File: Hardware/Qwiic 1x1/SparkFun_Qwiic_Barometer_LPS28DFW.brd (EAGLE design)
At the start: 25.4 x 25.4 mm, 48 parts, among them J1 QWIIC_RIGHT_ANGLE, J2 QWIIC_RIGHT_ANGLE, U1 LPS28DFW

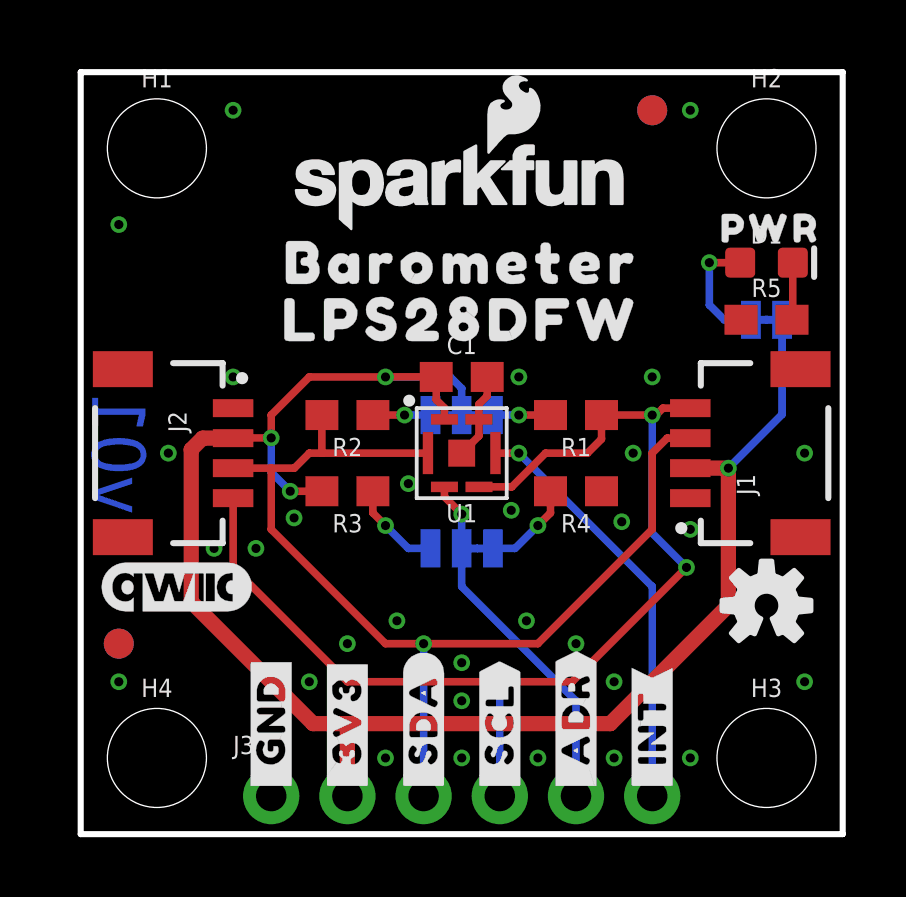
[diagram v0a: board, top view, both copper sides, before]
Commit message: Design review updates
Both:
Bump version number to v10
Change LPS28DF section name to "Barometer - LPS28DFW" in schematics
Remove SPI from ADR jumper in schematics
Add ordering instructions to boards

1x1:
Make SCL and SDA traces not overlap near Qwiic connector
Move OSHW down between connector and standoff
Move I@C jumper up to give more GND pour under sensor
Add SparkFun logo to bottom silk

Micro:
Space out test points in schematic
Add text about 22 AWG wires in schematic
Move OSHW logo up slightly to not clip at test points
Flip ADR labels to be correct
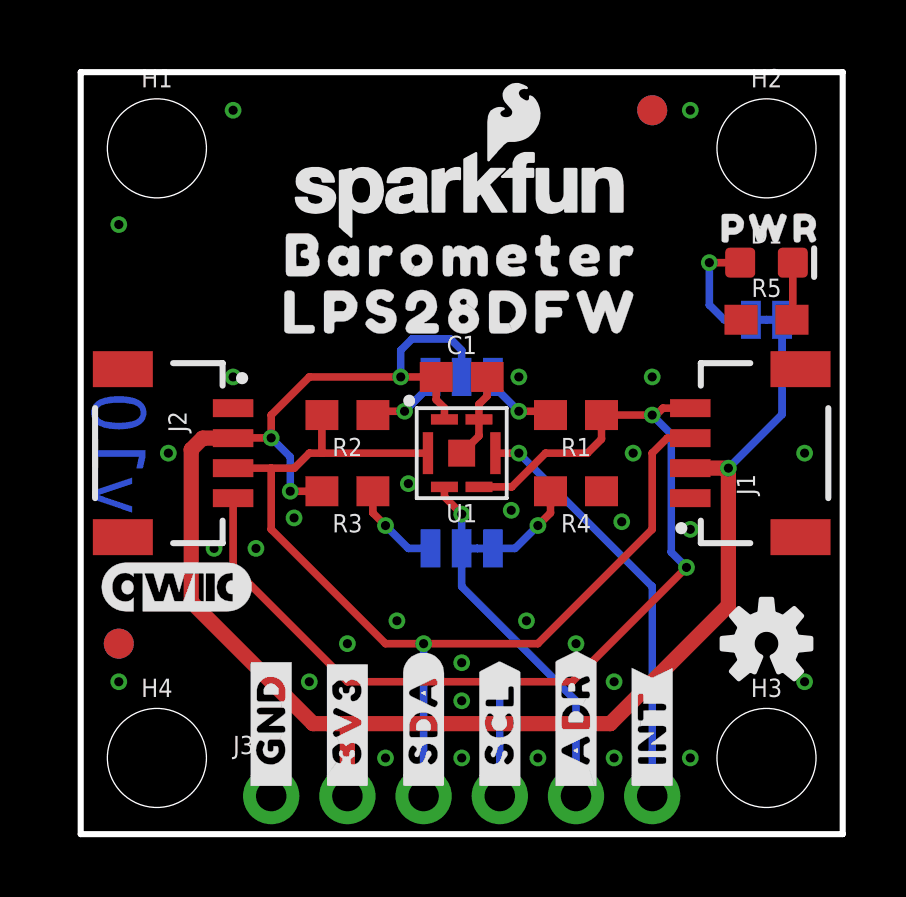
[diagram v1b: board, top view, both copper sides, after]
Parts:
- added LOGO4: SFE_LOGO_NAME_FLAME.1_INCH, SparkFun-Aesthetics:SFE_LOGO_NAME_FLAME_.1
- added U$19: (no value), SparkFun-Aesthetics:ORDERING_INSTRUCTIONS
- moved U$14 3.56 mm to (12.7, 19.3)
- moved U$15 3.56 mm to (12.7, 17.4)
- moved U$9 2.03 mm to (12.7, 13.6)
- moved LOGO1 1.27 mm to (22.9, 6.35)
- moved I2C 1.27 mm to (12.7, 15.2)
- moved U$13 1.09 mm to (22.9, 16.5), turned to 90 degrees
- moved LOGO3 0.25 mm to (12.7, 21.3)
- moved U$12 0.25 mm to (12.7, 17.4)
- moved U$11 0.25 mm to (12.7, 19.3)
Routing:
- net N$3: track 1.92 -> 2.61 mm
- net N$2: track 1.92 -> 2.61 mm
- net 3.3V: track 58.1 -> 58.6 mm
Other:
- board text added: "1.6mm Thickness"
- board text added: "2-Layer"
- board text added: "Lead-Free HASL"
- board text added: "v10"
- board text removed: "v01"
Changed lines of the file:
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@@
 <text x="-17.78" y="-2.54" size="1.778" layer="47" font="vector" ratio="15">Units: inches</text>
 <text x="16.51" y="-29.21" size="1.778" layer="51" font="vector">Dryw Wade</text>
-<text x="1.27" y="12.7" size="1.778" layer="16" font="vector" ratio="15" rot="MR270" align="center">v01</text>
+<text x="1.27" y="12.7" size="1.778" layer="16" font="vector" ratio="15" rot="MR270" align="center">v10</text>
+<text x="29.21" y="38.1" size="2.54" layer="51" font="vector">2-Layer</text>
+<text x="29.21" y="34.29" size="2.54" layer="51" font="vector">1.6mm Thickness</text>
+<text x="29.21" y="30.48" size="2.54" layer="51" font="vector">Lead-Free HASL</text>
 </plain>
 <attributes>
@@
 <attribute name="VALUE" x="5.08" y="-0.762" size="0.6096" layer="27" font="vector" ratio="20"/>
 </element>
-<element name="LOGO1" library="SparkFun-Aesthetics" package="OSHW-LOGO-S" value="OSHW-LOGOS" x="22.86" y="7.62" smashed="yes"/>
+<element name="LOGO1" library="SparkFun-Aesthetics" package="OSHW-LOGO-S" value="OSHW-LOGOS" x="22.86" y="6.35" smashed="yes"/>
 <element name="LOGO2" library="SparkFun-Aesthetics" package="QWIIC_5MM" value="QWIIC_LOGO_5MM" x="3.175" y="8.255" smashed="yes"/>
-<element name="LOGO3" library="SparkFun-Aesthetics" package="SFE_LOGO_NAME_FLAME_.1" value="SFE_LOGO_NAME_FLAME.1_INCH" x="12.7" y="21.59" smashed="yes"/>
+<element name="LOGO3" library="SparkFun-Aesthetics" package="SFE_LOGO_NAME_FLAME_.1" value="SFE_LOGO_NAME_FLAME.1_INCH" x="12.7" y="21.336" smashed="yes"/>
 <element name="U1" library="LPS28DFW" package="LPS28DFW" value="LPS28DFW" x="12.7" y="12.7" smashed="yes" rot="R180">
 <attribute name="NAME" x="12.7" y="10.7" size="0.6096" layer="25" font="vector" ratio="20" rot="R180" align="center"/>
@@
 <attribute name="VALUE" x="22.86" y="18.415" size="0.6096" layer="27" font="vector" ratio="20" align="top-center"/>
 </element>
-<element name="I2C" library="SparkFun-Jumpers" package="SMT-JUMPER_3_2-NC_TRACE_SILK" package3d_urn="urn:adsk.eagle:package:39289/1" value="JUMPER-SMT_3_2-NC_TRACE_SILK" x="12.7" y="13.97" smashed="yes" rot="MR180">
-<attribute name="NAME" x="12.7" y="12.827" size="0.6096" layer="26" font="vector" ratio="20" rot="MR180" align="bottom-center"/>
-<attribute name="VALUE" x="12.7" y="15.113" size="0.6096" layer="28" font="vector" ratio="20" rot="MR180" align="top-center"/>
+<element name="I2C" library="SparkFun-Jumpers" package="SMT-JUMPER_3_2-NC_TRACE_SILK" package3d_urn="urn:adsk.eagle:package:39289/1" value="JUMPER-SMT_3_2-NC_TRACE_SILK" x="12.7" y="15.24" smashed="yes" rot="MR180">
+<attribute name="NAME" x="12.7" y="14.097" size="0.6096" layer="26" font="vector" ratio="20" rot="MR180" align="bottom-center"/>
+<attribute name="VALUE" x="12.7" y="16.383" size="0.6096" layer="28" font="vector" ratio="20" rot="MR180" align="top-center"/>
 </element>
 <element name="ADR" library="SparkFun-Jumpers" package="SMT-JUMPER_3_1-NC_TRACE_SILK" package3d_urn="urn:adsk.eagle:package:39288/1" value="JUMPER-SMT_3_1-NC_TRACE_SILK" x="12.7" y="9.525" smashed="yes" rot="MR180">
@@
 <element name="U$7" library="output" package="#_SCL#0" value="" x="13.97" y="1.27" smashed="yes" rot="R90"/>
 <element name="U$8" library="output" package="#_SCL#0" value="" x="13.97" y="1.27" smashed="yes" rot="MR90"/>
-<element name="U$9" library="output" package="#I2C#0" value="" x="12.7" y="15.621" smashed="yes" rot="MR0"/>
+<element name="U$9" library="output" package="#I2C#0" value="" x="12.7" y="13.589" smashed="yes" rot="MR0"/>
 <element name="U$10" library="output" package="#ADR#0" value="" x="12.7" y="7.874" smashed="yes" rot="MR0"/>
-<element name="U$11" library="output" package="BAROMETER0" value="" x="12.7" y="19.05" smashed="yes"/>
-<element name="U$12" library="output" package="LPS28DFW0" value="" x="12.7" y="17.145" smashed="yes"/>
-<element name="U$13" library="output" package="#PWR#0" value="" x="21.971" y="17.145" smashed="yes" rot="MR0"/>
-<element name="U$14" library="output" package="BAROMETER0" value="" x="12.7" y="22.86" smashed="yes" rot="MR0"/>
-<element name="U$15" library="output" package="LPS28DFW0" value="" x="12.7" y="20.955" smashed="yes" rot="MR0"/>
+<element name="U$11" library="output" package="BAROMETER0" value="" x="12.7" y="19.304" smashed="yes"/>
+<element name="U$12" library="output" package="LPS28DFW0" value="" x="12.7" y="17.399" smashed="yes"/>
+<element name="U$13" library="output" package="#PWR#0" value="" x="22.86" y="16.51" smashed="yes" rot="MR90"/>
+<element name="U$14" library="output" package="BAROMETER0" value="" x="12.7" y="19.304" smashed="yes" rot="MR0"/>
+<element name="U$15" library="output" package="LPS28DFW0" value="" x="12.7" y="17.399" smashed="yes" rot="MR0"/>
 <element name="U$16" library="output" package="#0X5D#0" value="" x="11.303" y="9.525" smashed="yes" rot="MR0"/>
 <element name="U$17" library="output" package="#0X5C#0" value="" x="14.097" y="9.525" smashed="yes" rot="MR0"/>
@@
 <element name="U$23" library="output" package="#_ADR#0" value="" x="16.51" y="1.27" smashed="yes" rot="MR90"/>
 <element name="U$18" library="output" package="PWR0" value="" x="22.987" y="20.193" smashed="yes"/>
+<element name="LOGO4" library="SparkFun-Aesthetics" package="SFE_LOGO_NAME_FLAME_.1" value="SFE_LOGO_NAME_FLAME.1_INCH" x="12.7" y="21.336" smashed="yes" rot="MR0"/>
+<element name="U$19" library="SparkFun-Aesthetics" package="ORDERING_INSTRUCTIONS" value="" x="27.94" y="50.8" smashed="yes"/>
 </elements>
 <signals>
@@
 <wire x1="8.04" y1="11.43" x2="6.985" y2="11.43" width="0.254" layer="1"/>
 <via x="6.985" y="11.43" extent="1-16" drill="0.3048"/>
-<wire x1="6.985" y1="11.43" x2="6.35" y2="12.065" width="0.254" layer="16"/>
-<wire x1="6.35" y1="12.065" x2="6.35" y2="13.208" width="0.254" layer="16"/>
+<wire x1="6.985" y1="12.573" x2="6.35" y2="13.208" width="0.254" layer="16"/>
+<wire x1="6.985" y1="12.573" x2="6.985" y2="11.43" width="0.254" layer="16"/>
 <via x="6.35" y="13.208" extent="1-16" drill="0.3048"/>
 <wire x1="6.35" y1="13.208" x2="5.088" y2="13.208" width="0.254" layer="1"/>
 <wire x1="5.088" y1="13.208" x2="5.08" y2="13.2" width="0.254" layer="1"/>
-<via x="10.16" y="15.24" extent="1-16" drill="0.3048"/>
-<wire x1="10.16" y1="15.24" x2="11.85" y2="15.24" width="0.254" layer="1"/>
-<wire x1="12.319" y1="15.24" x2="12.7" y2="14.859" width="0.254" layer="16"/>
-<wire x1="12.7" y1="14.859" x2="12.7" y2="13.97" width="0.254" layer="16"/>
-<wire x1="10.16" y1="15.24" x2="12.319" y2="15.24" width="0.254" layer="16"/>
+<via x="10.668" y="15.24" extent="1-16" drill="0.3048"/>
+<wire x1="10.668" y1="15.24" x2="11.85" y2="15.24" width="0.254" layer="1"/>
 <wire x1="6.35" y1="13.208" x2="6.35" y2="13.97" width="0.254" layer="1"/>
 <wire x1="6.35" y1="13.97" x2="7.62" y2="15.24" width="0.254" layer="1"/>
-<wire x1="7.62" y1="15.24" x2="10.16" y2="15.24" width="0.254" layer="1"/>
+<wire x1="7.62" y1="15.24" x2="10.668" y2="15.24" width="0.254" layer="1"/>
 <via x="21.59" y="12.2" extent="1-16" drill="0.3048"/>
 <wire x1="21.59" y1="12.2" x2="23.3807" y2="13.9907" width="0.254" layer="16"/>
 <wire x1="23.3807" y1="13.9907" x2="23.3807" y2="17.145" width="0.254" layer="16"/>
+<wire x1="10.668" y1="15.24" x2="10.668" y2="16.129" width="0.254" layer="16"/>
+<wire x1="11.049" y1="16.51" x2="10.668" y2="16.129" width="0.254" layer="16"/>
+<wire x1="11.049" y1="16.51" x2="12.319" y2="16.51" width="0.254" layer="16"/>
+<wire x1="12.319" y1="16.51" x2="12.7" y2="16.129" width="0.254" layer="16"/>
+<wire x1="12.7" y1="16.129" x2="12.7" y2="15.24" width="0.254" layer="16"/>
 </signal>
 <signal name="SDA">
@@
 <wire x1="5.08" y1="8.89" x2="8.89" y2="5.08" width="0.254" layer="1"/>
 <via x="20.193" y="8.89" extent="1-16" drill="0.3048"/>
-<wire x1="20.193" y1="8.89" x2="19.05" y2="10.033" width="0.254" layer="16"/>
-<wire x1="19.05" y1="10.033" x2="19.05" y2="13.97" width="0.254" layer="16"/>
+<wire x1="20.193" y1="8.89" x2="19.685" y2="9.398" width="0.254" layer="16"/>
+<wire x1="19.685" y1="13.335" x2="19.05" y2="13.97" width="0.254" layer="16"/>
+<wire x1="19.685" y1="13.335" x2="19.685" y2="9.398" width="0.254" layer="16"/>
 <via x="19.05" y="13.97" extent="1-16" drill="0.3048"/>
 <wire x1="19.05" y1="13.97" x2="17.36" y2="13.97" width="0.254" layer="1"/>
@@
 <contactref element="R1" pad="2"/>
 <contactref element="I2C" pad="3"/>
-<wire x1="15.66" y1="13.97" x2="14.605" y2="13.97" width="0.254" layer="1"/>
-<via x="14.605" y="13.97" extent="1-16" drill="0.3048"/>
-<wire x1="14.605" y1="13.97" x2="13.7414" y2="13.97" width="0.254" layer="16"/>
+<wire x1="15.66" y1="13.97" x2="15.533" y2="14.097" width="0.254" layer="1"/>
+<wire x1="15.533" y1="14.097" x2="14.605" y2="14.097" width="0.254" layer="1"/>
+<via x="14.605" y="14.097" extent="1-16" drill="0.3048"/>
+<wire x1="14.605" y1="14.097" x2="13.7414" y2="14.9606" width="0.254" layer="16"/>
+<wire x1="13.7414" y1="15.24" x2="13.7414" y2="14.9606" width="0.254" layer="16"/>
 </signal>
 <signal name="N$3">
 <contactref element="R2" pad="1"/>
 <contactref element="I2C" pad="1"/>
-<wire x1="9.74" y1="13.97" x2="10.795" y2="13.97" width="0.254" layer="1"/>
-<via x="10.795" y="13.97" extent="1-16" drill="0.3048"/>
-<wire x1="10.795" y1="13.97" x2="11.6586" y2="13.97" width="0.254" layer="16"/>
+<wire x1="10.795" y1="14.097" x2="9.867" y2="14.097" width="0.254" layer="1"/>
+<wire x1="9.74" y1="13.97" x2="9.867" y2="14.097" width="0.254" layer="1"/>
+<via x="10.795" y="14.097" extent="1-16" drill="0.3048"/>
+<wire x1="11.6586" y1="15.24" x2="11.6586" y2="14.9606" width="0.254" layer="16"/>
+<wire x1="10.795" y1="14.097" x2="11.6586" y2="14.9606" width="0.254" layer="16"/>
 </signal>
 <signal name="N$5">

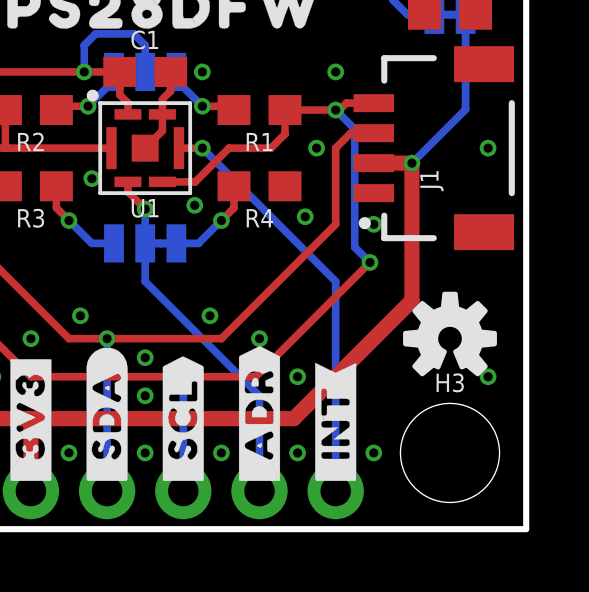
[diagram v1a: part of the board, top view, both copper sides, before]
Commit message: Move OSHW logo in 1x1
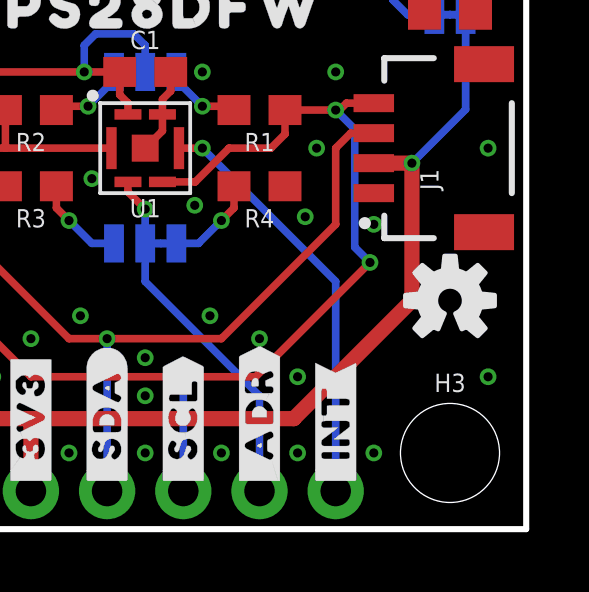
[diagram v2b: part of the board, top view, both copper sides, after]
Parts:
- moved LOGO1 1.27 mm to (22.9, 7.62)
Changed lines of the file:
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@@
 <attribute name="VALUE" x="5.08" y="-0.762" size="0.6096" layer="27" font="vector" ratio="20"/>
 </element>
-<element name="LOGO1" library="SparkFun-Aesthetics" package="OSHW-LOGO-S" value="OSHW-LOGOS" x="22.86" y="6.35" smashed="yes"/>
+<element name="LOGO1" library="SparkFun-Aesthetics" package="OSHW-LOGO-S" value="OSHW-LOGOS" x="22.86" y="7.62" smashed="yes"/>
 <element name="LOGO2" library="SparkFun-Aesthetics" package="QWIIC_5MM" value="QWIIC_LOGO_5MM" x="3.175" y="8.255" smashed="yes"/>
 <element name="LOGO3" library="SparkFun-Aesthetics" package="SFE_LOGO_NAME_FLAME_.1" value="SFE_LOGO_NAME_FLAME.1_INCH" x="12.7" y="21.336" smashed="yes"/>

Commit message: Remove library file
Part is in SFE Eagle library, update part in design
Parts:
- U1: device LPS28DFW:LPS28DFW -> SparkFun-Sensors:CCLGA-7L
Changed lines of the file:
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@@
 <element name="LOGO2" library="SparkFun-Aesthetics" package="QWIIC_5MM" value="QWIIC_LOGO_5MM" x="3.175" y="8.255" smashed="yes"/>
 <element name="LOGO3" library="SparkFun-Aesthetics" package="SFE_LOGO_NAME_FLAME_.1" value="SFE_LOGO_NAME_FLAME.1_INCH" x="12.7" y="21.336" smashed="yes"/>
-<element name="U1" library="LPS28DFW" package="LPS28DFW" value="LPS28DFW" x="12.7" y="12.7" smashed="yes" rot="R180">
+<element name="U1" library="SparkFun-Sensors" package="CCLGA-7L" value="LPS28DFW" x="12.7" y="12.7" smashed="yes" rot="R180">
 <attribute name="NAME" x="12.7" y="10.7" size="0.6096" layer="25" font="vector" ratio="20" rot="R180" align="center"/>
 <attribute name="PROD_ID" value="IC-17197" x="12.7" y="12.7" size="1.778" layer="27" rot="R180" display="off"/>
